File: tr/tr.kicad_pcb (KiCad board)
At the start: 4 copper layers, 104.4 x 65.5 mm, 97 parts, among them J1 SMA, J2 SMA, J3 SMA, K1 CONN_3, Q1 Si7850, Q3 STD2NK90ZT4, Q4 STD2NK90ZT4, T1 DA2033-AL_, U1 L6388E, U2 LT1631, U3 LT3757

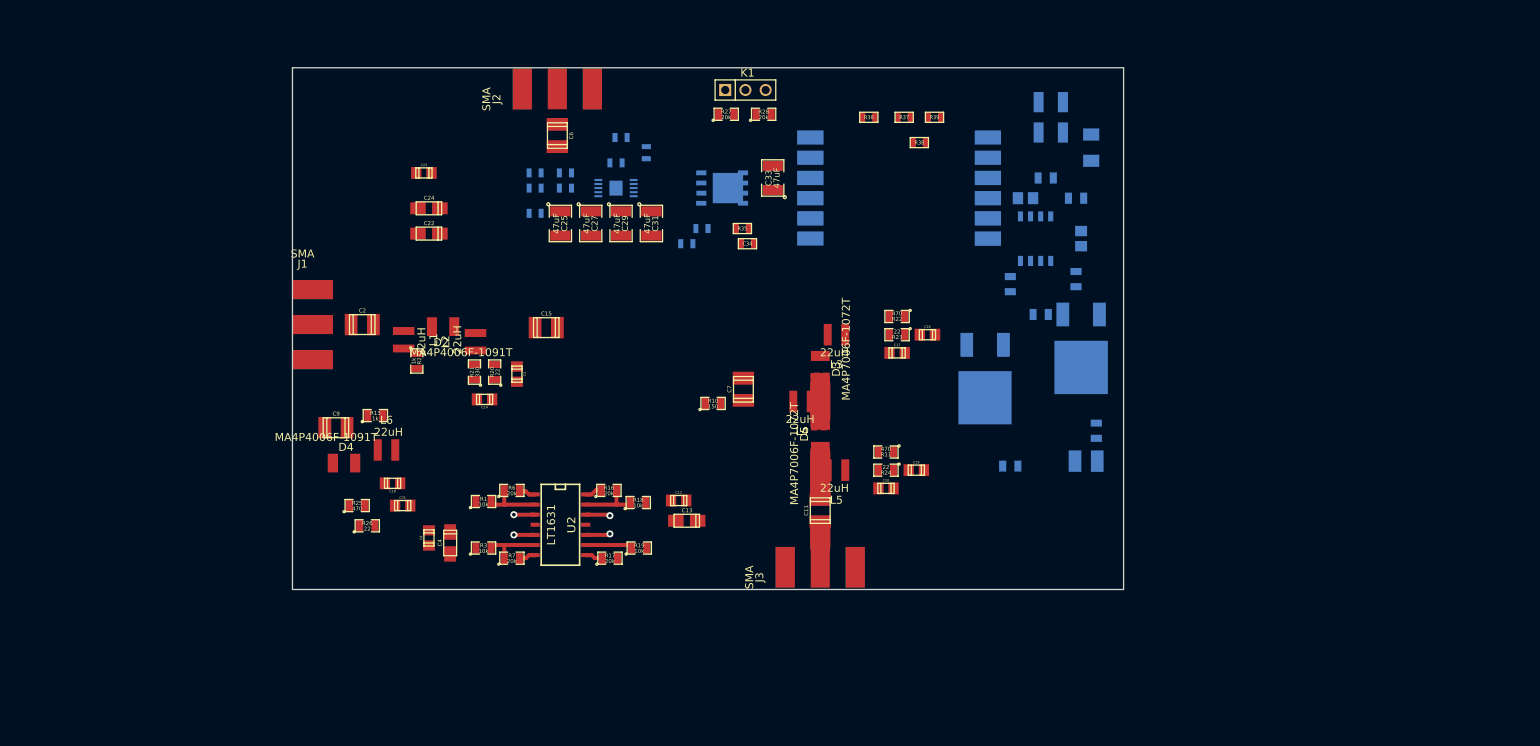
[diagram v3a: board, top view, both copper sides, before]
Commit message: routing for high voltage power supply
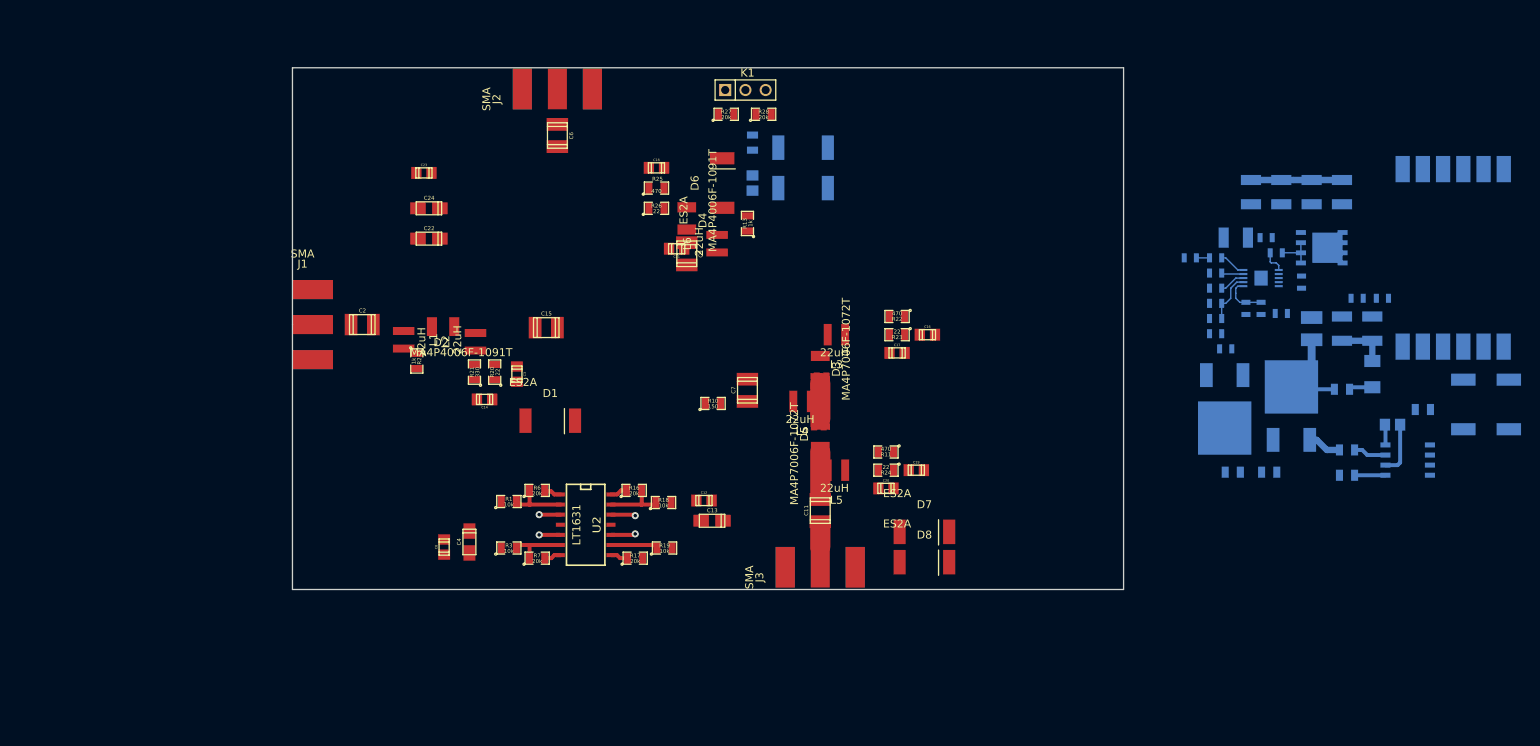
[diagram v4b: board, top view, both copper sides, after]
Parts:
- added D1: ES2A, SMB_DO2144AA, F.Cu at (89.5, 69.2)
- added D10: ES2A, SMB_DO2144AA, B.Cu at (121.3, 34.9)
- added D11: ES2G-E3/52T, SMB_DO2144AA, B.Cu at (209.9, 67.2)
- added D12: ES2G-E3/52T, SMB_DO2144AA, B.Cu at (204.2, 67.2)
- added D6: ES2A, SMB_DO2144AA, F.Cu at (111.1, 39.4)
- added D7: ES2A, SMB_DO2144AA, F.Cu at (136.5, 83.2)
- added D8: ES2A, SMB_DO2144AA, F.Cu at (136.5, 87.0)
- added D9: ES2A, SMB_DO2144AA, B.Cu at (121.3, 40.0)
- C25, C27, C29, C31, C33, C34, R35, R36, R37, R38, R39: moved to B.Cu
- moved C25 98.2 mm to (189.0, 40.5)
- moved C28 95.0 mm to (181.4, 55.8), turned to 180 degrees
- moved R29 92.8 mm to (178.8, 55.1), turned to 90 degrees
- moved C27 90.6 mm to (185.2, 40.5)
- moved C26 90.1 mm to (176.9, 55.1), turned to 90 degrees
- moved C29 83.0 mm to (181.4, 40.5)
- moved C30 82.9 mm to (173.1, 52.6)
- moved R30 82.4 mm to (173.1, 50.7)
- moved C32 82.0 mm to (179.5, 46.2)
- moved U3 81.8 mm to (178.8, 51.3)
- moved R35 80.9 mm to (194.1, 53.8)
- moved C34 76.9 mm to (190.9, 53.8), turned to 0 degrees
- moved R31 76.3 mm to (173.1, 48.8), turned to 0 degrees
- moved Q1 75.7 mm to (186.4, 47.5)
- moved R34 75.6 mm to (183.9, 51.8), turned to 90 degrees
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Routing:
- net VDD: track 0.00 -> 12.5 mm
- net VCC: track 0.00 -> 11.4 mm
- net /hvout: track 0.00 -> 6.74 mm
- net N-0000046: track 0.00 -> 6.48 mm
- net N-0000036: track 0.00 -> 6.35 mm
- net N-0000049: track 0.00 -> 5.71 mm
- net N-0000034: track 0.00 -> 4.89 mm
- net N-0000028: track 0.00 -> 4.26 mm
- net N-0000057: track 0.00 -> 4.14 mm
- net N-0000027: track 0.00 -> 3.87 mm
- net N-0000044: track 0.00 -> 3.36 mm
- net N-0000052: track 0.00 -> 3.26 mm
- net N-0000050: track 0.00 -> 2.98 mm
- net N-0000032: track 0.00 -> 2.96 mm
- net N-0000043: track 0.00 -> 2.78 mm
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- added copper zone on F.Cu, net N-0000034
- removed copper zone on F.Cu, net N-0000034 (its old number)
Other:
- net class Default: clearance 0.254 -> 0.17; trace_width 0.254 -> 0.18
- net class hv: clearance 2 -> 0.5
- rule trace_clearance: 0.254 -> 0.17
- rule trace_min: 0.254 -> 0.17

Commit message: work on transmitter layout
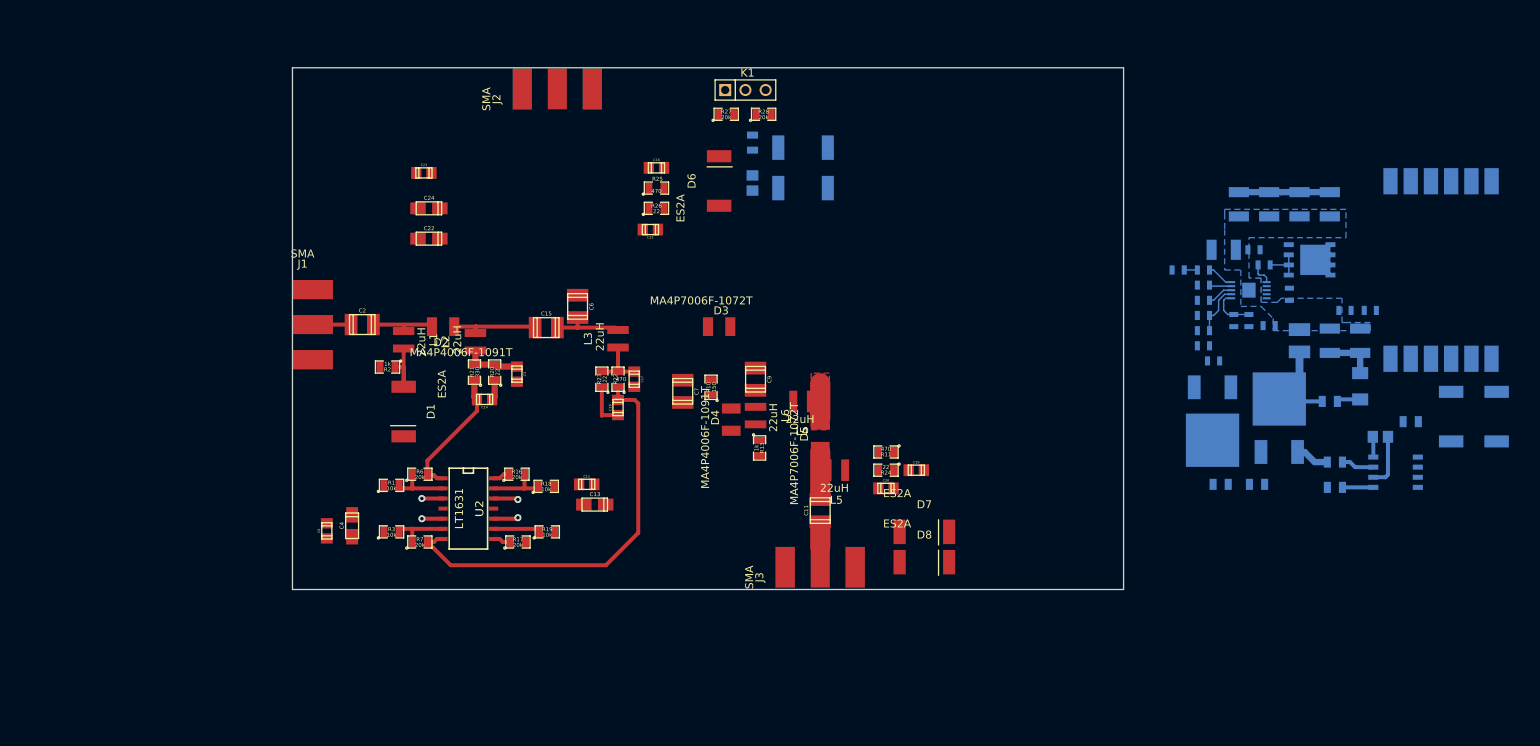
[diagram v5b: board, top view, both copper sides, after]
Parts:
- moved C16 39.9 mm to (98.0, 67.6), turned to 90 degrees
- moved R23 37.5 mm to (96.0, 64.0), turned to 90 degrees
- moved R22 35.9 mm to (98.0, 64.0), turned to 90 degrees
- moved C17 33.2 mm to (100.1, 64.0), turned to 270 degrees
- moved R13 28.2 mm to (115.8, 72.6), turned to 270 degrees
- moved L3 27.4 mm to (98.0, 58.9), turned to 90 degrees
- moved D4 25.9 mm to (112.3, 69.1), turned to 90 degrees
- moved L6 22.1 mm to (115.3, 68.6), turned to 270 degrees
- moved C6 21.6 mm to (93.0, 54.9)
- moved D1 18.5 mm to (71.1, 68.1), turned to 270 degrees
- moved C9 18.0 mm to (115.3, 64.0)
- moved C12 14.9 mm to (94.1, 77.2)
- moved U2 14.9 mm to (79.4, 80.3)
- moved C13 14.9 mm to (95.1, 79.8)
- moved C4 14.9 mm to (64.6, 82.4)
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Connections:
- C14 pad 1: N-000008 (its old number) -> /OUTA
- C16 pad 1: N-0000016 (its old number) -> /OUTB
- C21 pad 1: N-0000010 -> /OUTD
- R17 pad 1: N-0000013 (its old number) -> /OUTC
- R21 pad 1: N-000008 (its old number) -> /OUTA
- R22 pad 1: N-0000016 (its old number) -> /OUTB
- R25 pad 1: N-0000010 -> /OUTD
- R7 pad 2: N-000005 -> /OUTB
- U2 pad 7: N-000005 -> /OUTB
- U2 pad 8: N-0000013 (its old number) -> /OUTC
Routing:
- net /OUTB: track 0.00 -> 52.1 mm
- net /OUTA: track 2.18 -> 16.8 mm
- net N-0000029: track 0.00 -> 11.1 mm
- net N-0000058: track 0.00 -> 9.27 mm
- net N-0000021: track 0.00 -> 8.36 mm
- net N-0000019: track 0.00 -> 8.02 mm
- net N-0000016: track 0.00 -> 7.25 mm
- net N-0000013: track 0.00 -> 7.09 mm
- net N-0000011: track 0.00 -> 5.68 mm
- net N-0000020: track 0.00 -> 4.83 mm
- net N-0000015: track 0.00 -> 2.61 mm
- net N-0000013 (its old number): track 2.25 -> 0.00 mm
- net /OUTC: track 0.00 -> 2.25 mm
- net N-000005: track 2.13 -> 0.00 mm
- added copper zone on B.Cu, net GND
- added copper zone on F.Cu, net N-0000034
- removed copper zone on F.Cu, net N-0000032

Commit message: updated layout of tr
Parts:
- C1, D10, D9, R12: moved to F.Cu
- C7, R10: moved to B.Cu
- moved K1 74.3 mm to (59.9, 78.6), turned to 270 degrees
- moved D10 71.4 mm to (71.6, 86.2)
- moved R28 67.2 mm to (79.2, 86.7), turned to 180 degrees
- moved R10 62.1 mm to (171.7, 69.0), turned to 180 degrees
- moved C7 61.3 mm to (167.4, 68.1), turned to 90 degrees
- moved D9 60.3 mm to (71.6, 74.3)
- moved R12 59.7 mm to (67.2, 70.2)
- moved C1 54.5 mm to (67.2, 65.8)
- moved R27 53.3 mm to (79.3, 73.1)
- moved C23 50.1 mm to (106.4, 76.0), turned to 180 degrees
- moved C24 44.8 mm to (106.9, 73.3), turned to 180 degrees
- moved C22 35.8 mm to (66.7, 81.3), turned to 90 degrees
- moved C18 30.0 mm to (103.4, 67.4), turned to 90 degrees
- moved D6 28.3 mm to (108.9, 67.3), turned to 270 degrees
- moved R25 27.6 mm to (99.4, 67.4), turned to 90 degrees
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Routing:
- net /OUTB: track 52.1 -> 4.38 mm
- net N-0000056: track 9.91 -> 23.0 mm
- net VDD: track 12.5 -> 0.00 mm
- net /OUTA: track 16.8 -> 4.79 mm
- net N-0000057: track 0.00 -> 8.45 mm
- net N-0000018: track 5.71 -> 12.4 mm
- net N-000007: track 0.00 -> 5.71 mm
- net N-0000023: track 0.00 -> 5.27 mm
- net N-0000026: track 4.26 -> 0.00 mm
- net N-0000029: track 11.1 -> 7.41 mm
- net N-0000011: track 5.68 -> 2.59 mm
- net N-0000030: track 2.96 -> 0.00 mm
- net N-0000022: track 0.00 -> 2.49 mm
- net /OUTC: track 2.25 -> 4.38 mm
- net N-0000014: track 0.00 -> 2.12 mm
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- removed copper zone on F.Cu, net N-0000034

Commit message: transmitter layout
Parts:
- C10, C25, C26, C27, C28, C29, C30, C31, C32, C33, C34, C35, C36, C5, C7, D11, D12, Q1, Q3, Q4, R10, R14, R15, R29, R30, R31, R32, R33, R34, R35, R36, R37, R38, R39, R4, R40, R5, R8, R9, T1, U1, U3: moved to F.Cu
- moved D11 101.7 mm to (109.6, 47.2), turned to 0 degrees
- moved D12 86.5 mm to (120.1, 47.2), turned to 0 degrees
- moved C25 85.8 mm to (99.9, 29.6), turned to 180 degrees
- moved T1 83.0 mm to (117.6, 35.9), turned to 180 degrees
- moved C27 82.0 mm to (99.9, 33.4), turned to 180 degrees
- moved C29 78.4 mm to (99.9, 37.2), turned to 180 degrees
- moved C31 75.0 mm to (99.9, 41.0), turned to 180 degrees
- moved R14 70.4 mm to (127.6, 52.0), turned to 180 degrees
- moved U1 64.6 mm to (130.6, 56.5)
- moved C5 60.9 mm to (132.5, 52.0), turned to 0 degrees
- moved R35 57.1 mm to (134.3, 35.5), turned to 180 degrees
- moved C35 55.5 mm to (134.5, 41.0)
- moved R40 55.5 mm to (134.5, 46.7)
- moved C34 50.9 mm to (137.5, 35.5), turned to 180 degrees
- moved R4 49.7 mm to (138.2, 55.2), turned to 0 degrees
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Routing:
- net GND: track 11.5 -> 93.0 mm, vias 4 -> 30
- net N-0000027: track 0.00 -> 49.7 mm
- net /hvbias: track 0.00 -> 46.6 mm, vias 0 -> 2
- net /OUTC: track 4.38 -> 44.6 mm
- net VCC: track 11.4 -> 46.4 mm
- net N-0000038: track 0.00 -> 34.9 mm
- net N-0000034: track 6.35 -> 34.2 mm, vias 0 -> 2
- net N-0000017: track 0.00 -> 27.2 mm
- net /OUTB: track 4.38 -> 28.6 mm
- net /hvout: track 6.74 -> 27.8 mm
- net /OUTD: track 4.26 -> 17.6 mm
- net VDD: track 0.00 -> 12.1 mm
- net /OUTA: track 4.79 -> 15.2 mm
- net VEE: track 0.00 -> 9.04 mm
- net /TX: track 0.00 -> 7.90 mm
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- added copper zone on F.Cu, net GND
- added copper zone on F.Cu, net N-0000038
- removed copper zone on B.Cu, net GND

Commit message: t/r vcc layout
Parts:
- moved K1 97.1 mm to (157.0, 82.3)
- moved R12 74.2 mm to (140.7, 74.2), turned to 180 degrees
- moved R28 73.3 mm to (152.4, 84.2), turned to 270 degrees
- moved R27 70.7 mm to (149.6, 80.6), turned to 270 degrees
- moved D9 68.8 mm to (140.2, 80.3), turned to 90 degrees
- moved D10 63.8 mm to (135.1, 80.3), turned to 90 degrees
- moved C1 59.0 mm to (125.2, 54.6), turned to 270 degrees
- moved C24 41.1 mm to (78.0, 44.1), turned to 270 degrees
- moved C22 39.7 mm to (80.4, 44.1), turned to 270 degrees
- moved C23 39.0 mm to (82.9, 44.8), turned to 270 degrees
- moved R14 23.1 mm to (134.1, 74.2), turned to 0 degrees
- moved C4 2.31 mm to (70.6, 79.1)
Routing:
- net VCC: track 46.4 -> 294.9 mm, vias 0 -> 12
- net /RX: track 6.91 -> 107.9 mm, vias 0 -> 3
- net /TX: track 7.90 -> 105.4 mm, vias 0 -> 3
- net GND: track 93.0 -> 132.6 mm, vias 30 -> 43
- net N-0000040: track 2.39 -> 29.5 mm
- net N-0000039: track 0.00 -> 25.2 mm
- net N-0000043: track 1.65 -> 19.5 mm, vias 0 -> 2
- net /OUTC: track 44.6 -> 40.9 mm
- net N-000004: track 5.94 -> 8.72 mm
- net /hvbias: track 46.6 -> 46.1 mm
